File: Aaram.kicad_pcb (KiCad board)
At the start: 2 copper layers, 100 x 100 mm, 52 parts, among them J1 Conn_01x03, J2 Conn_01x02, J3 AC_OUT, J4 SWITCH_IN, J5 PSU_OUT, J6 PSU_AC_IN, J8 SPARE_PINS, K1 10A cube relay, K2 10A cube relay, K3 10A cube relay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

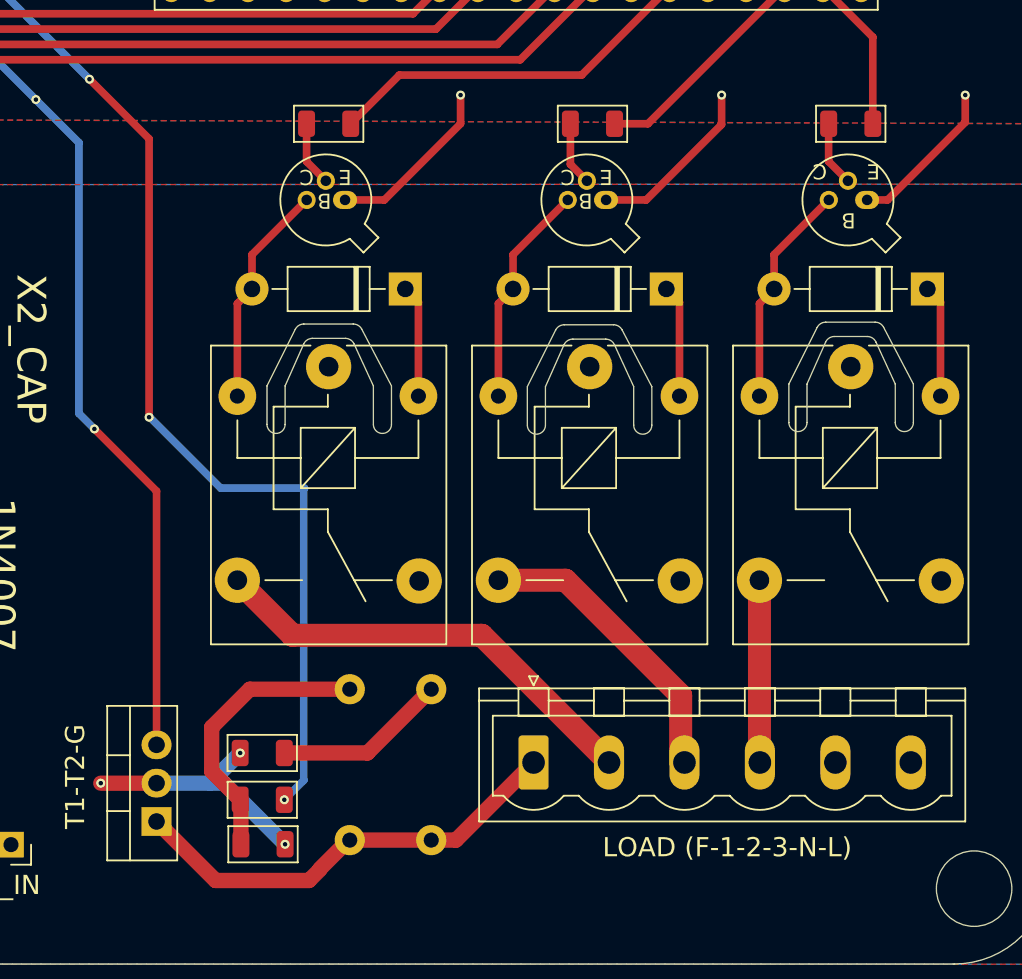
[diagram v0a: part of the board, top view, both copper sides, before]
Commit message: Added 5v connection to relays
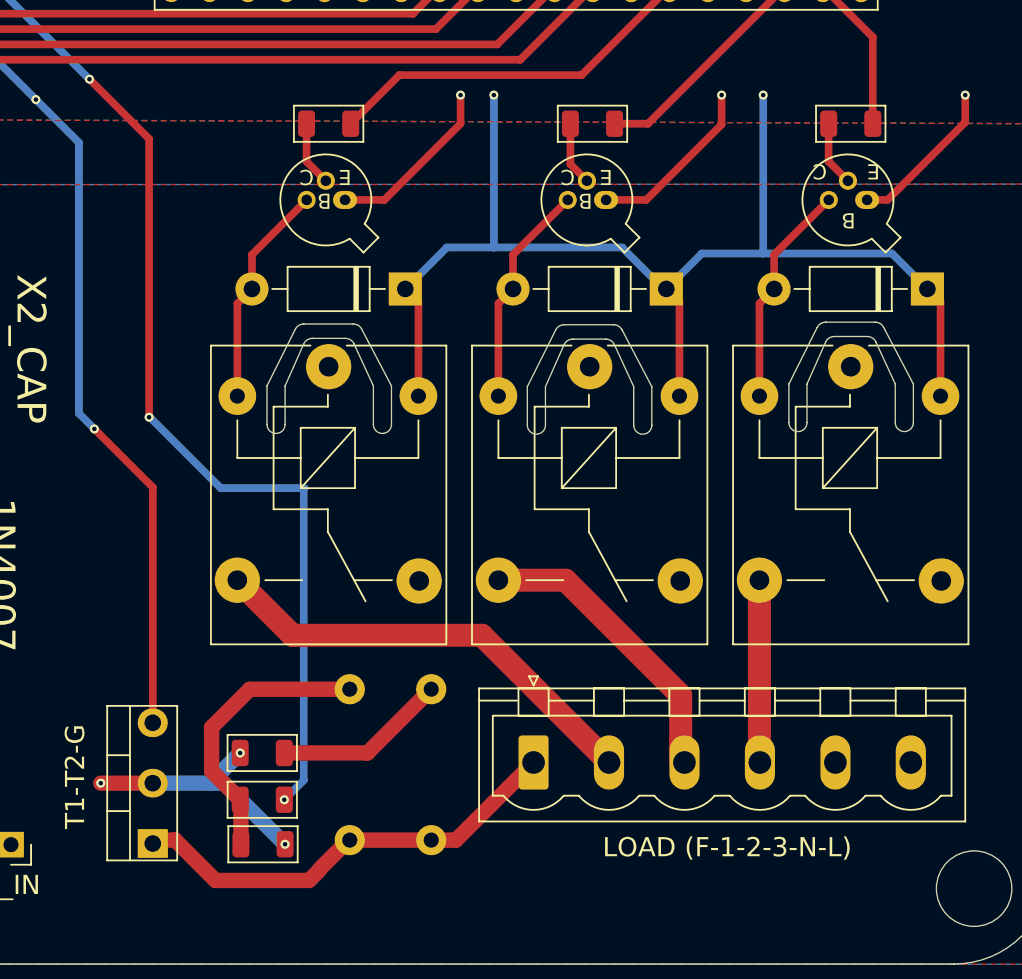
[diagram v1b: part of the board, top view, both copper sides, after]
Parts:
- J5: value PSU_OUT -> 5V_OUT
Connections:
- D1 pad 1: Net-(D1-K) -> +5V
- D2 pad 1: Net-(D2-K) -> +5V
- D3 pad 1: Net-(D3-K) -> +5V
- K1 pad 5: Net-(D1-K) -> +5V
- K2 pad 5: Net-(D3-K) -> +5V
- K3 pad 5: Net-(D2-K) -> +5V
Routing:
- net +5V: track 14.4 -> 96.2 mm, vias 0 -> 2
- net Net-(D2-K): track 7.46 -> 0.00 mm
- net Net-(D3-K): track 7.46 -> 0.00 mm
- net Net-(D1-K): track 7.46 -> 0.00 mm
- net Net-(Q1-G): track 60.1 -> 58.8 mm
